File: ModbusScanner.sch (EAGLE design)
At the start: 6 parts, among them IC1 MAX481CPA, X0 PN61729-S, X1 Modbus, X2 LCD (I2C), X3 Pot

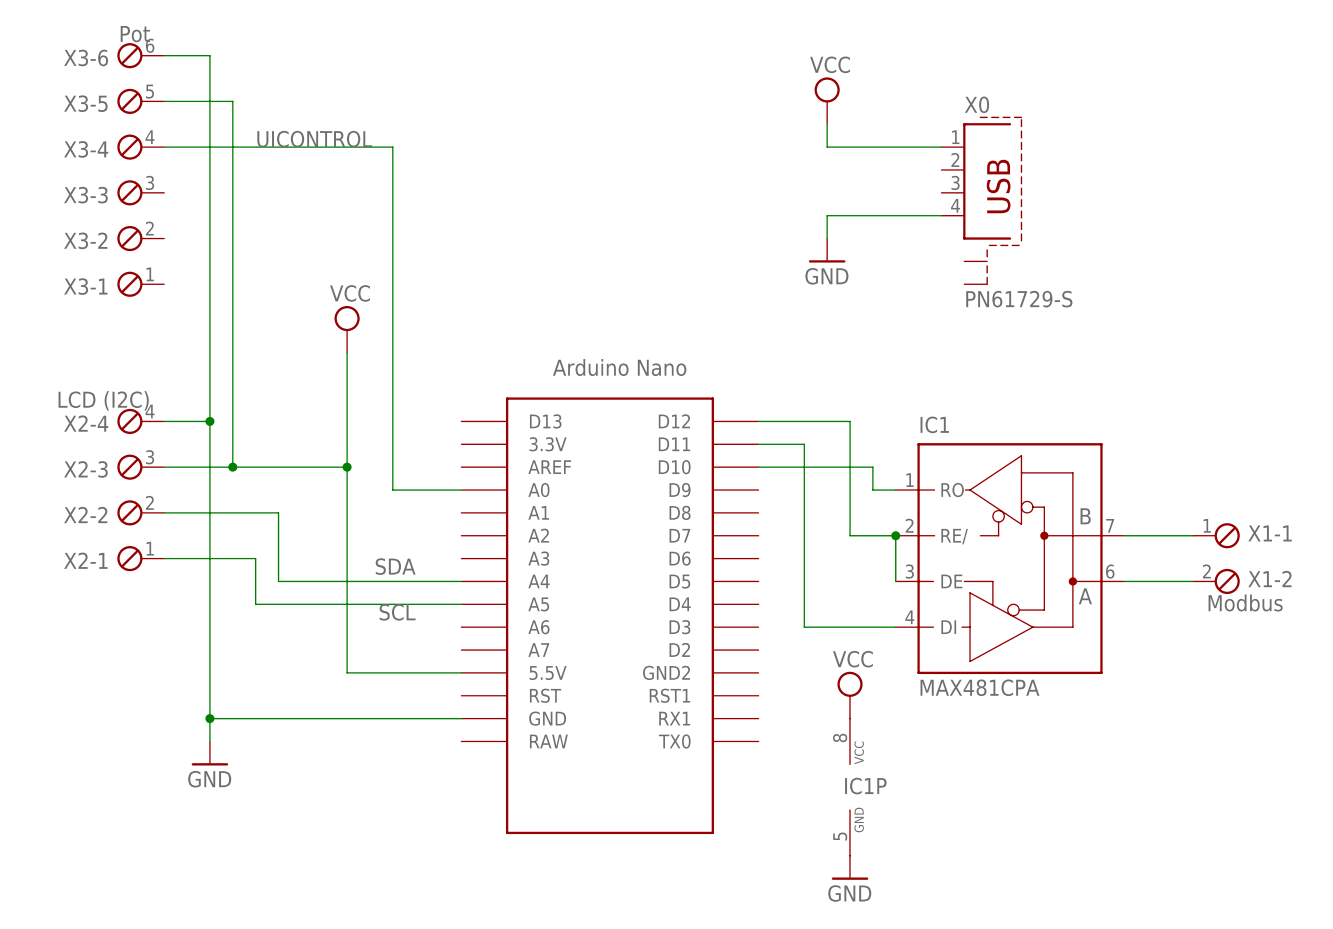
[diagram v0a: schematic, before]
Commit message: updated circuit diagram
replaced pot with encoder
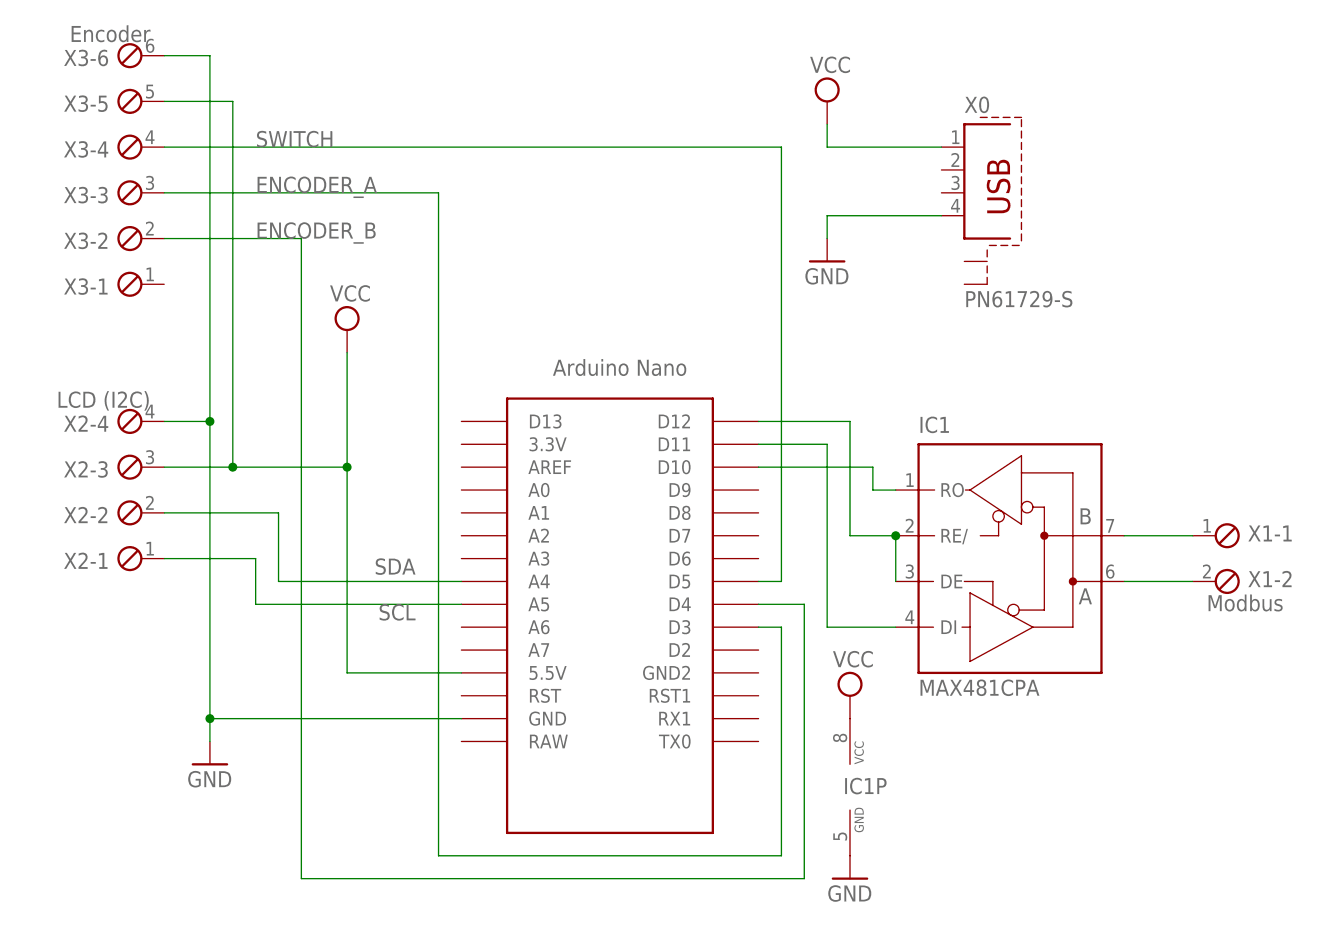
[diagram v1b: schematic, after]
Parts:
- X3: value Pot -> Encoder
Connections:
- removed net UICONTROL: U$1.A0, X3-4.1
- new net ENCODER_A: U$1.D3, X3-3.1
- new net ENCODER_B: U$1.D4, X3-2.1
- new net SWITCH: U$1.D5, X3-4.1
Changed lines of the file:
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@@
 <part name="SUPPLY5" library="supply2" deviceset="VCC" device=""/>
 <part name="SUPPLY6" library="supply2" deviceset="VCC" device=""/>
-<part name="X3" library="con-phoenix-254" deviceset="MPT6" device="" value="Pot"/>
+<part name="X3" library="con-phoenix-254" deviceset="MPT6" device="" value="Encoder"/>
 </parts>
 <sheets>
@@
 <segment>
 <pinref part="IC1" gate="G$1" pin="DI"/>
-<wire x1="73.66" y1="35.56" x2="63.5" y2="35.56" width="0.1524" layer="91"/>
-<wire x1="63.5" y1="35.56" x2="63.5" y2="55.88" width="0.1524" layer="91"/>
+<wire x1="73.66" y1="35.56" x2="66.04" y2="35.56" width="0.1524" layer="91"/>
+<wire x1="66.04" y1="35.56" x2="66.04" y2="55.88" width="0.1524" layer="91"/>
 <pinref part="U$1" gate="G$1" pin="D11"/>
-<wire x1="63.5" y1="55.88" x2="58.42" y2="55.88" width="0.1524" layer="91"/>
+<wire x1="66.04" y1="55.88" x2="58.42" y2="55.88" width="0.1524" layer="91"/>
 </segment>
 </net>
@@
 </segment>
 </net>
-<net name="UICONTROL" class="0">
+<net name="SWITCH" class="0">
 <segment>
 <pinref part="X3" gate="-4" pin="1"/>
-<wire x1="-7.62" y1="88.9" x2="17.78" y2="88.9" width="0.1524" layer="91"/>
-<wire x1="17.78" y1="88.9" x2="17.78" y2="50.8" width="0.1524" layer="91"/>
-<pinref part="U$1" gate="G$1" pin="A0"/>
-<wire x1="17.78" y1="50.8" x2="25.4" y2="50.8" width="0.1524" layer="91"/>
+<wire x1="-7.62" y1="88.9" x2="60.96" y2="88.9" width="0.1524" layer="91"/>
 <label x="2.54" y="88.9" size="1.778" layer="95"/>
+<wire x1="60.96" y1="88.9" x2="60.96" y2="40.64" width="0.1524" layer="91"/>
+<pinref part="U$1" gate="G$1" pin="D5"/>
+<wire x1="60.96" y1="40.64" x2="58.42" y2="40.64" width="0.1524" layer="91"/>
 </segment>
 </net>
+<net name="ENCODER_A" class="0">
+<segment>
+<pinref part="X3" gate="-3" pin="1"/>
+<wire x1="-7.62" y1="83.82" x2="22.86" y2="83.82" width="0.1524" layer="91"/>
+<wire x1="22.86" y1="83.82" x2="22.86" y2="10.16" width="0.1524" layer="91"/>
+<wire x1="22.86" y1="10.16" x2="60.96" y2="10.16" width="0.1524" layer="91"/>
+<wire x1="60.96" y1="10.16" x2="60.96" y2="35.56" width="0.1524" layer="91"/>
+<pinref part="U$1" gate="G$1" pin="D3"/>
+<wire x1="60.96" y1="35.56" x2="58.42" y2="35.56" width="0.1524" layer="91"/>
+<label x="2.54" y="83.82" size="1.778" layer="95"/>
+</segment>
+</net>
+<net name="ENCODER_B" class="0">
+<segment>
+<pinref part="X3" gate="-2" pin="1"/>
+<wire x1="-7.62" y1="78.74" x2="7.62" y2="78.74" width="0.1524" layer="91"/>
+<wire x1="7.62" y1="78.74" x2="7.62" y2="7.62" width="0.1524" layer="91"/>
+<wire x1="7.62" y1="7.62" x2="63.5" y2="7.62" width="0.1524" layer="91"/>
+<wire x1="63.5" y1="7.62" x2="63.5" y2="38.1" width="0.1524" layer="91"/>
+<pinref part="U$1" gate="G$1" pin="D4"/>
+<wire x1="63.5" y1="38.1" x2="58.42" y2="38.1" width="0.1524" layer="91"/>
+<label x="2.54" y="78.74" size="1.778" layer="95"/>
+</segment>
+</net>
